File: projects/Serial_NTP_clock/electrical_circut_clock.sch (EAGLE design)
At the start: 37 parts, among them IC1 74HC595N, IC2 7805T, IC3 LD117AV, J1 DCJ0202

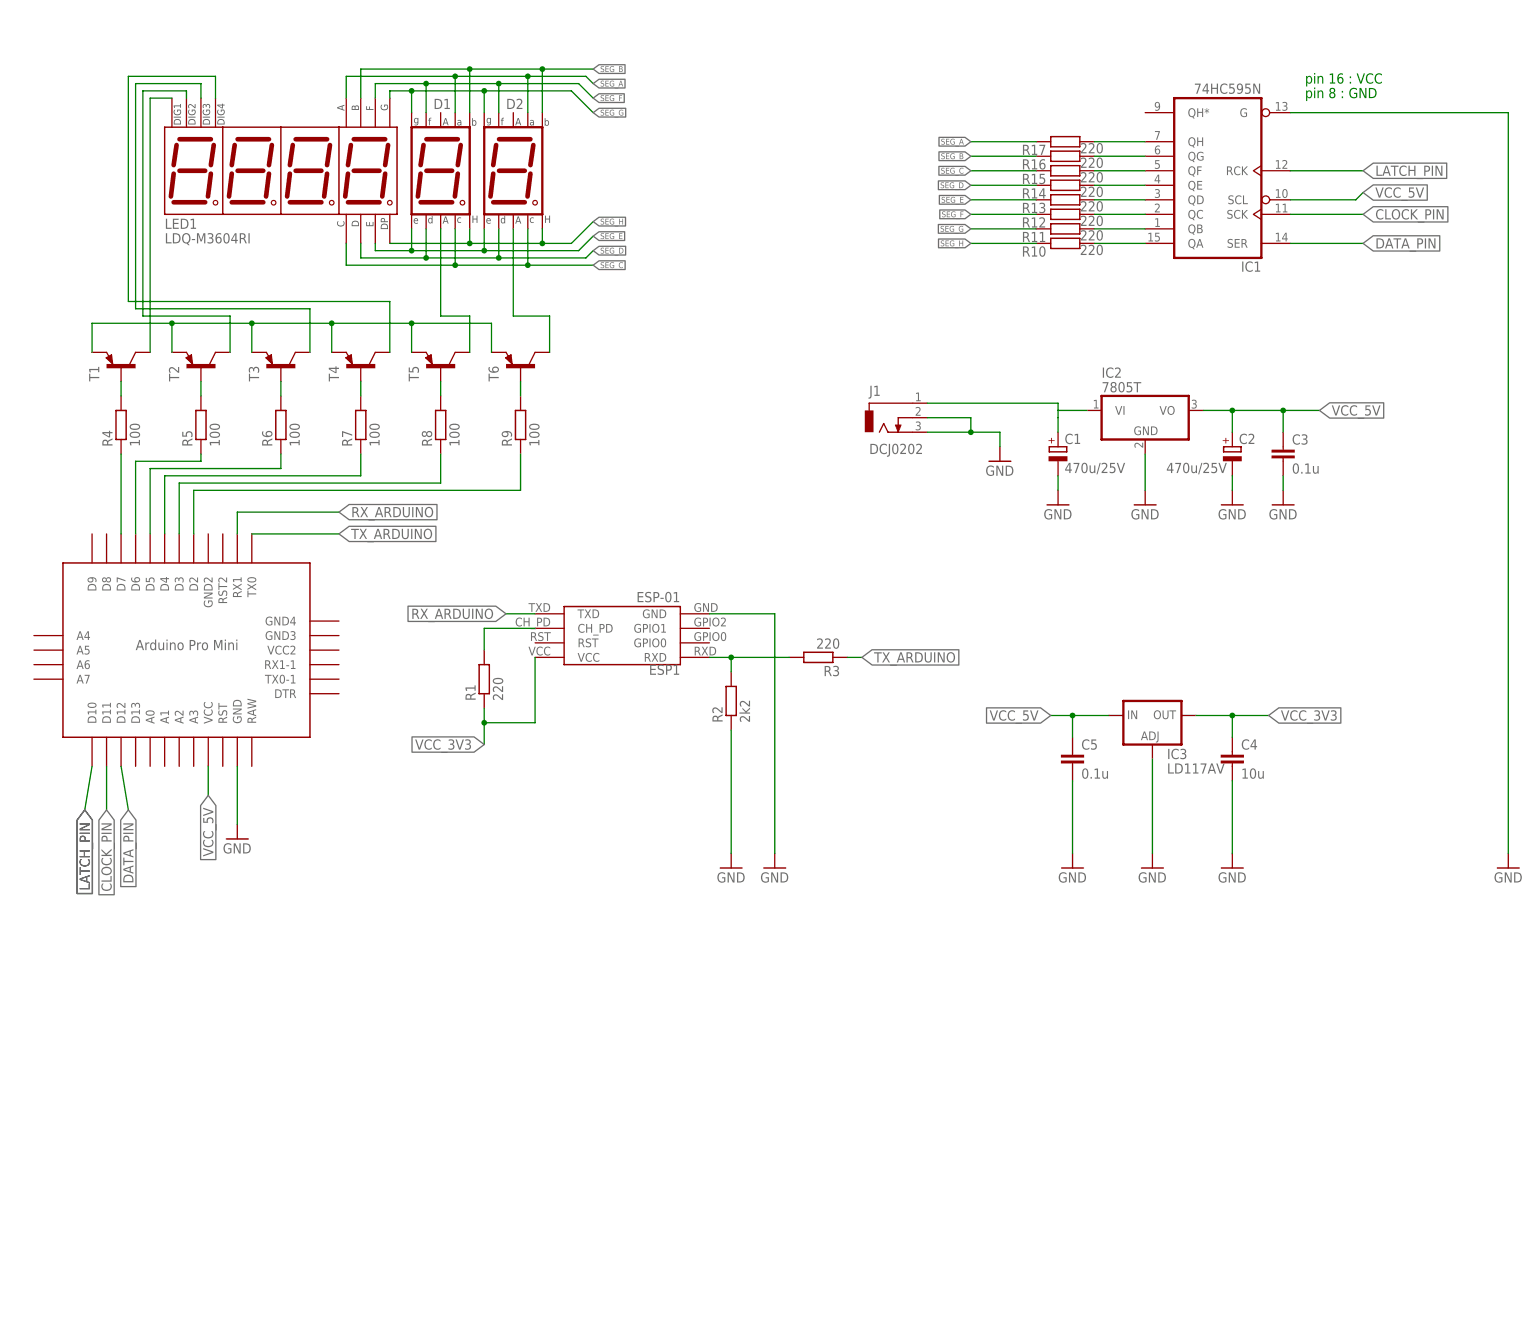
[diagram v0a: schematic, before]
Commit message: Grounded plate, relocated module of scheme and added more vias
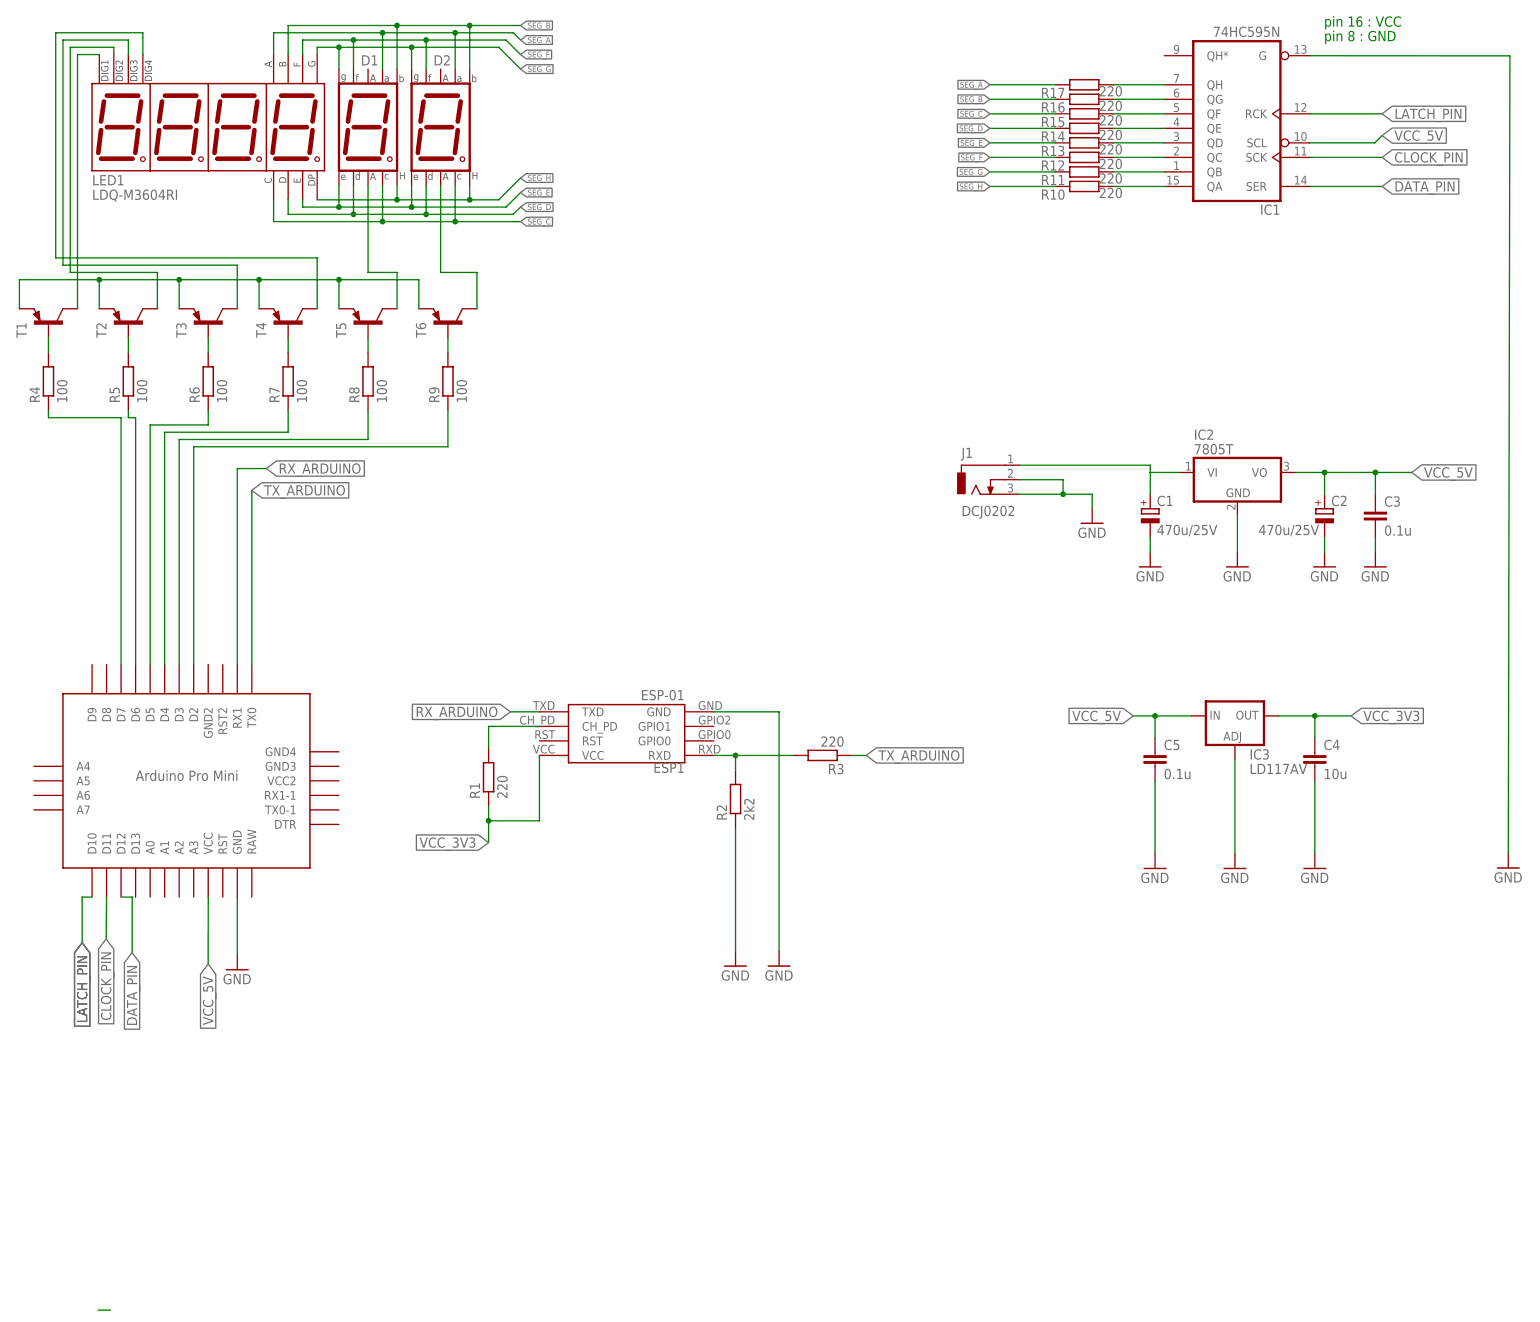
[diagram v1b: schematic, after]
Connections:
- new net N$11: U$1.D12
- net DATA_PIN: no longer U$1.D12
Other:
- moved on the sheet: C1, C2, C3, C4, C5, D1, D2, ESP1, IC1, IC2, IC3, J1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

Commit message: fixed consistency problems
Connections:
- removed net N$11: U$1.D12
- net DATA_PIN: now also U$1.D12
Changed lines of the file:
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@@
 <setting verticaltext="up"/>
 </settings>
-<grid distance="1" unitdist="mil" unit="mil" style="lines" multiple="1" display="no" altdistance="0.01" altunitdist="inch" altunit="inch"/>
+<grid distance="50" unitdist="mil" unit="mil" style="lines" multiple="1" display="no" altdistance="0.01" altunitdist="inch" altunit="inch"/>
 <layers>
 <layer number="1" name="Top" color="4" fill="1" visible="no" active="no"/>
@@
 <net name="DATA_PIN" class="0">
 <segment>
-<label x="26.0478" y="30.9406" size="1.778" layer="95" rot="R270" xref="yes"/>
 <wire x1="20.1676" y1="-31.5976" x2="22.2758" y2="-31.5976" width="0.1524" layer="91"/>
 </segment>
@@
 <label x="244.6274" y="164.8968" size="1.778" layer="95" xref="yes"/>
 </segment>
+<segment>
+<pinref part="U$1" gate="G$1" pin="D12"/>
+<wire x1="24.13" y1="40.64" x2="24.13" y2="39.37" width="0.1524" layer="91"/>
+<wire x1="24.13" y1="39.37" x2="27.94" y2="39.37" width="0.1524" layer="91"/>
+<wire x1="27.94" y1="39.37" x2="27.94" y2="30.48" width="0.1524" layer="91"/>
+<label x="27.94" y="30.48" size="1.778" layer="95" rot="R270" xref="yes"/>
+</segment>
 </net>
 <net name="CLOCK_PIN" class="0">
-<segment>
-<wire x1="21.59" y1="40.64" x2="21.5202" y2="33.3152" width="0.1524" layer="91"/>
-<label x="21.5202" y="33.3152" size="1.778" layer="95" rot="R270" xref="yes"/>
-<pinref part="U$1" gate="G$1" pin="D11"/>
-</segment>
 <segment>
 <pinref part="IC1" gate="A" pin="SCK"/>
@@
 <label x="244.6274" y="169.9768" size="1.778" layer="95" xref="yes"/>
 </segment>
+<segment>
+<pinref part="U$1" gate="G$1" pin="D11"/>
+<wire x1="21.59" y1="40.64" x2="21.59" y2="30.48" width="0.1524" layer="91"/>
+<label x="21.59" y="30.48" size="1.778" layer="95" rot="R270" xref="yes"/>
+</segment>
 </net>
 <net name="LATCH_PIN" class="0">
-<segment>
-<label x="17.3228" y="32.6644" size="1.778" layer="95" rot="R270" xref="yes"/>
-<label x="17.3228" y="32.6644" size="1.778" layer="95" rot="R270" xref="yes"/>
-<pinref part="U$1" gate="G$1" pin="D10"/>
-<wire x1="19.05" y1="40.64" x2="17.3228" y2="40.64" width="0.1524" layer="91"/>
-<wire x1="17.3228" y1="40.64" x2="17.3228" y2="32.639" width="0.1524" layer="91"/>
-</segment>
 <segment>
 <pinref part="IC1" gate="A" pin="RCK"/>
 <wire x1="231.9274" y1="177.5968" x2="244.6274" y2="177.5968" width="0.1524" layer="91"/>
 <label x="244.6274" y="177.5968" size="1.778" layer="95" xref="yes"/>
+</segment>
+<segment>
+<pinref part="U$1" gate="G$1" pin="D10"/>
+<wire x1="19.05" y1="40.64" x2="13.97" y2="40.64" width="0.1524" layer="91"/>
+<wire x1="13.97" y1="40.64" x2="13.97" y2="30.48" width="0.1524" layer="91"/>
+<label x="13.97" y="30.48" size="1.778" layer="95" rot="R270" xref="yes"/>
 </segment>
 </net>
@@
 </segment>
 </net>
-<net name="N$11" class="0">
-<segment>
-<pinref part="U$1" gate="G$1" pin="D12"/>
-<wire x1="24.13" y1="40.64" x2="26.0604" y2="40.64" width="0.1524" layer="91"/>
-<wire x1="26.0604" y1="40.64" x2="26.0604" y2="30.9626" width="0.1524" layer="91"/>
-</segment>
-</net>
